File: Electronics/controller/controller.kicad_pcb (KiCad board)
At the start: 2 copper layers, 23 parts, among them P3 PANEL_2, P4 PANEL_1, P5 DIAL, P6 POWER, P7 SWITCH, P8 LED_DISPLAY, Q1 BUZ11, U1 LM317T, U2 74HC595, U3 Arduino_Pro_Micro

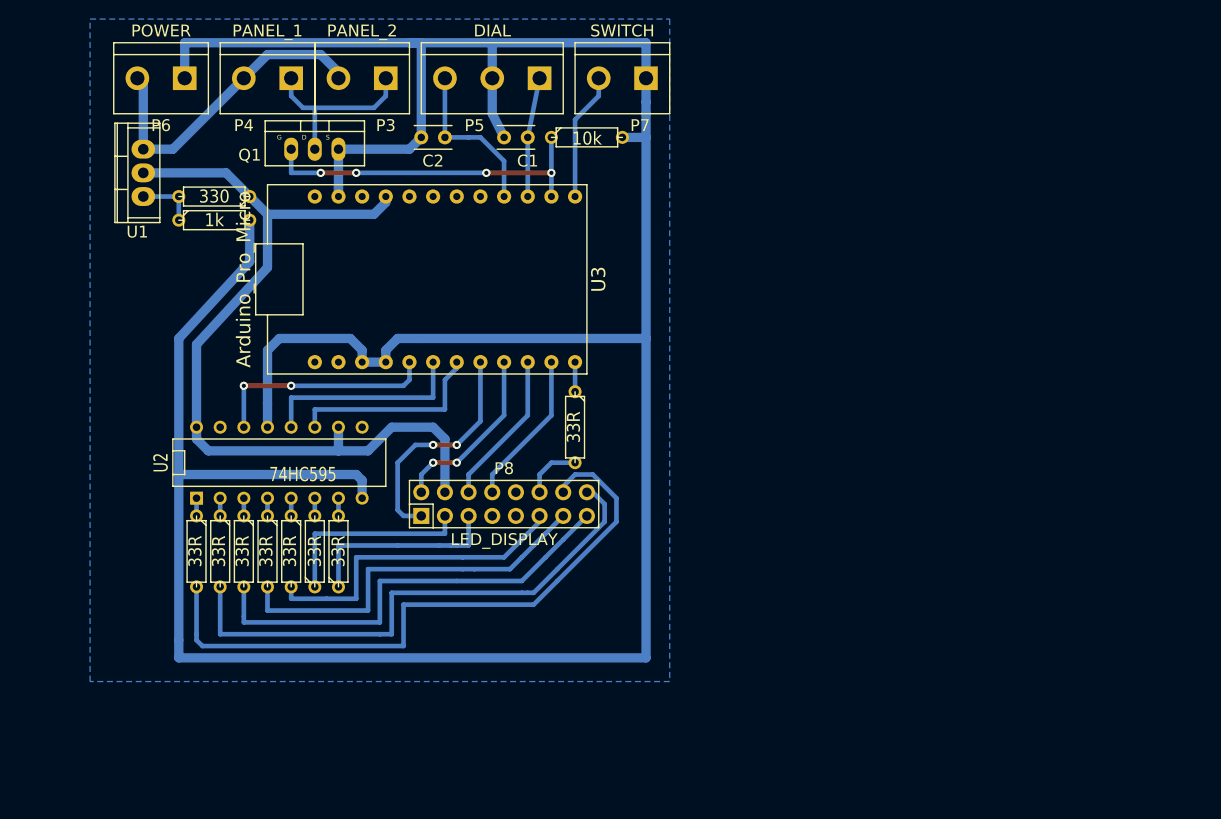
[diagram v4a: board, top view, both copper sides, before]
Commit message: Renumbered some sockets. Rerouted pins.
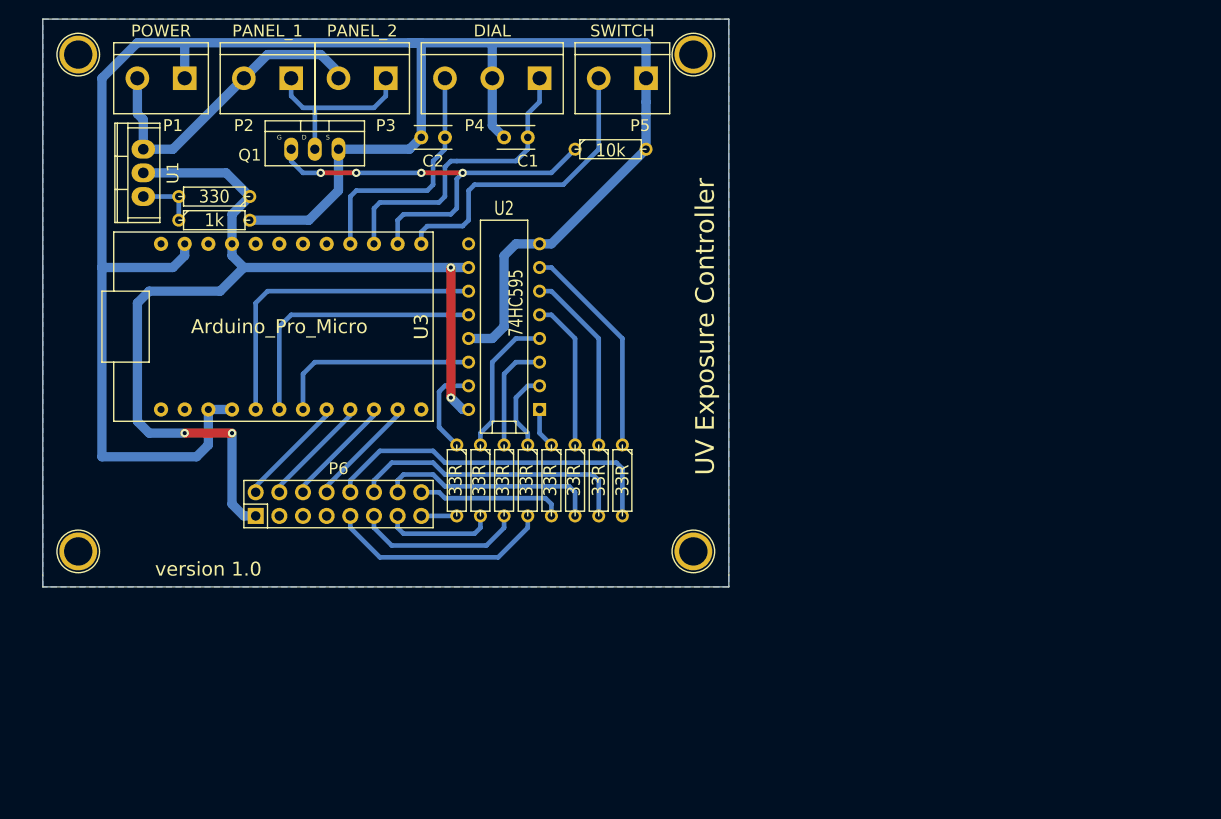
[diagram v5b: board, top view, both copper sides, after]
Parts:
- removed P8: LED_DISPLAY, Pin_Headers:Pin_Header_Straight_2x08
- removed the R10 at (161.3, 95.9)
- removed the R2 at (133.3, 109.2)
- removed the R3 at (135.9, 109.2)
- added 1PIN: P***, Connect:1pin, F.Cu at (174.0, 55.9)
- added 1PIN: P***, Connect:1pin, F.Cu at (108.0, 55.9)
- added 1PIN: P***, Connect:1pin, F.Cu at (174.0, 109.2)
- added 1PIN: P***, Connect:1pin, F.Cu at (108.0, 109.2)
- added P6: LED_DISPLAY, Pin_Headers:Pin_Header_Straight_2x08, F.Cu at (135.9, 104.1)
- added R1: 33R, Discret:R3, F.Cu at (148.6, 101.6)
- added R7: 33R, Discret:R3, F.Cu at (163.8, 101.6)
- added R8: 33R, Discret:R3, F.Cu at (166.4, 101.6)
- moved R6 41.3 mm to (161.3, 101.6)
- moved R5 36.4 mm to (158.8, 101.6)
- moved R3 29.0 mm to (153.7, 101.6)
- moved U2 28.2 mm to (153.7, 85.1), turned to 90 degrees
- moved R4 26.5 mm to (156.2, 101.6)
- moved R2 24.1 mm to (151.1, 101.6)
- moved U3 17.3 mm to (121.9, 83.8)
- moved R9 2.84 mm to (165.1, 66.0)
- renumbered P6 to P1, P4 to P2, P5 to P4, P7 to P5, R5 to R10, R4 to R11, R9 to R2, R7 to R3, R11 to R4, R6 to R5, R8 to R6, R1 to R9
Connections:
- R2 pad 1: /C -> /D
- R3 pad 1: /G -> /C
- R4 pad 1: /F -> /B
- R5 pad 1: /B -> /A
- R6 pad 1: /A -> /E
- U2 pad 11: /D4 -> /D2
- U2 pad 14: /D2 -> /D4
- U2 pad 15: Net-(U2-Pad15) -> /COL
- U2 pad 3: /G -> /C
- U2 pad 4: /C -> /D
- U2 pad 5: /F -> /E
- U2 pad 6: /D -> /F
- U2 pad 7: /E -> /G
- U2 pad 9: Net-(U2-Pad9) -> (no net)
- U3 pad 1: Net-(U3-Pad1) -> (no net)
- U3 pad 10: /D7 -> /D6
- U3 pad 11: /D8 -> /D5
- U3 pad 12: /D9 -> (no net)
- U3 pad 17: Net-(U3-Pad17) -> (no net)
- U3 pad 18: Net-(U3-Pad18) -> (no net)
- U3 pad 19: Net-(U3-Pad19) -> (no net)
- U3 pad 2: Net-(U3-Pad2) -> (no net)
- U3 pad 20: Net-(U3-Pad20) -> (no net)
- U3 pad 22: Net-(U3-Pad22) -> (no net)
- U3 pad 24: Net-(U3-Pad24) -> (no net)
- U3 pad 8: /D5 -> /D8
- U3 pad 9: /D6 -> /D7
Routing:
- net GND: track 335.9 -> 224.3 mm
- net Net-(P6-Pad14): track 69.7 -> 23.9 mm
- net Net-(P6-Pad16): track 58.3 -> 15.8 mm
- net Net-(P6-Pad10): track 0.00 -> 37.7 mm
- net Net-(P6-Pad12): track 0.00 -> 31.1 mm
- net Net-(P6-Pad11): track 48.0 -> 18.1 mm
- net Net-(P6-Pad13): track 41.1 -> 12.0 mm
- net Net-(P8-Pad5): track 21.6 -> 0.00 mm
- net Net-(P8-Pad3): track 21.6 -> 0.00 mm
- net /G: track 1.91 -> 23.5 mm
- net /D14: track 12.8 -> 33.0 mm
- net /D10: track 13.8 -> 33.5 mm
- net /F: track 1.91 -> 19.9 mm
- net VCC: track 93.2 -> 109.0 mm, vias 0 -> 4
- net /E: track 1.91 -> 16.3 mm
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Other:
- board outline added: 73.7 x 61 mm
- board text added: "UV Exposure Controller"
- board text added: "version 1.0"

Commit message: Updates
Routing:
- net Net-(P6-Pad12): track 31.1 -> 27.7 mm
- net Net-(P6-Pad14): track 23.9 -> 21.6 mm
- net Net-(P6-Pad11): track 18.1 -> 16.1 mm
- net Net-(P6-Pad10): track 37.7 -> 35.8 mm
- net Net-(P6-Pad13): track 12.0 -> 10.4 mm
- net GND: track 224.3 -> 222.8 mm
- net Net-(P6-Pad9): track 24.2 -> 23.3 mm
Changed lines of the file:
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@@
     (links 54)
     (no_connects 0)
-    (area 99.735 48.3 182.205 116.8)
+    (area 104.089999 52.019999 177.850001 113.080001)
     (thickness 1.6)
     (drawings 10)
-    (tracks 229)
+    (tracks 226)
     (zones 0)
     (modules 27)
@@
     (pad_to_mask_clearance 0)
     (aux_axis_origin 0 0)
-    (visible_elements 7FFFEFFF)
+    (visible_elements 7FFFFFFF)
     (pcbplotparams
       (layerselection 0x00000_80000001)
@@
   (segment (start 158.75 76.2) (end 168.91 66.04) (width 1) (layer B.Cu) (net 1))
   (segment (start 124.46 93.98) (end 121.92 93.98) (width 1) (layer B.Cu) (net 1))
-  (segment (start 121.92 93.98) (end 121.92 97.79) (width 1) (layer B.Cu) (net 1))
-  (segment (start 121.92 97.79) (end 120.65 99.06) (width 1) (layer B.Cu) (net 1))
-  (segment (start 110.49 78.74) (end 110.49 99.06) (width 1) (layer B.Cu) (net 1))
-  (segment (start 110.49 99.06) (end 120.65 99.06) (width 1) (layer B.Cu) (net 1))
   (segment (start 119.38 76.2) (end 119.38 77.47) (width 1) (layer B.Cu) (net 1))
   (segment (start 118.11 78.74) (end 110.49 78.74) (width 1) (layer B.Cu) (net 1))
@@
   (segment (start 119.38 54.61) (end 119.38 58.42) (width 1) (layer B.Cu) (net 1) (status 20))
   (segment (start 168.91 66.04) (end 168.91 66.04) (width 1) (layer B.Cu) (net 1) (status 10))
-  (segment (start 168.91 62.23) (end 168.91 66.04) (width 1) (layer B.Cu) (net 1) (status 20))
-  (segment (start 168.91 60.96) (end 168.91 62.23) (width 1) (layer B.Cu) (net 1))
-  (segment (start 168.91 54.61) (end 168.91 60.96) (width 1) (layer B.Cu) (net 1))
-  (segment (start 152.4 54.61) (end 168.91 54.61) (width 1) (layer B.Cu) (net 1))
   (segment (start 168.91 66.04) (end 168.91 66.04) (width 1) (layer B.Cu) (net 1) (status 30))
   (segment (start 152.4 54.61) (end 143.51 54.61) (width 1) (layer B.Cu) (net 1))
+  (segment (start 121.92 97.79) (end 121.92 93.98) (width 1) (layer B.Cu) (net 1))
+  (segment (start 120.65 99.06) (end 121.92 97.79) (width 1) (layer B.Cu) (net 1))
+  (segment (start 111.76 99.06) (end 120.65 99.06) (width 1) (layer B.Cu) (net 1))
+  (segment (start 110.49 97.79) (end 111.76 99.06) (width 1) (layer B.Cu) (net 1))
+  (segment (start 110.49 78.74) (end 110.49 97.79) (width 1) (layer B.Cu) (net 1))
+  (segment (start 168.91 62.23) (end 168.91 66.04) (width 1) (layer B.Cu) (net 1))
+  (segment (start 168.91 55.88) (end 168.91 62.23) (width 1) (layer B.Cu) (net 1))
+  (segment (start 167.64 54.61) (end 168.91 55.88) (width 1) (layer B.Cu) (net 1))
+  (segment (start 152.4 54.61) (end 167.64 54.61) (width 1) (layer B.Cu) (net 1))
   (segment (start 149.86 81.28) (end 128.27 81.28) (width 0.5) (layer B.Cu) (net 2))
   (segment (start 128.27 81.28) (end 127 82.55) (width 0.5) (layer B.Cu) (net 2))
@@
   (segment (start 130.81 58.42) (end 130.81 60.325) (width 0.5) (layer B.Cu) (net 24))
   (segment (start 133.35 66.04) (end 133.35 61.595) (width 0.5) (layer B.Cu) (net 24))
-  (segment (start 137.16 105.41) (end 137.16 106.68) (width 0.5) (layer B.Cu) (net 25) (status 10))
+  (segment (start 137.16 106.68) (end 139.192 108.712) (width 0.5) (layer B.Cu) (net 25))
+  (segment (start 154.178 108.712) (end 156.21 106.68) (width 0.5) (layer B.Cu) (net 25))
+  (segment (start 137.16 105.41) (end 137.16 106.68) (width 0.5) (layer B.Cu) (net 25))
+  (segment (start 139.192 108.712) (end 154.178 108.712) (width 0.5) (layer B.Cu) (net 25))
   (segment (start 156.21 106.68) (end 156.21 105.41) (width 0.5) (layer B.Cu) (net 25))
-  (segment (start 153.035 109.855) (end 156.21 106.68) (width 0.5) (layer B.Cu) (net 25))
-  (segment (start 140.335 109.855) (end 153.035 109.855) (width 0.5) (layer B.Cu) (net 25))
-  (segment (start 137.16 106.68) (end 140.335 109.855) (width 0.5) (layer B.Cu) (net 25))
-  (segment (start 137.16 101.6) (end 137.16 102.87) (width 0.5) (layer B.Cu) (net 26) (status 20))
-  (segment (start 140.335 98.425) (end 137.16 101.6) (width 0.5) (layer B.Cu) (net 26))
-  (segment (start 146.05 98.425) (end 140.335 98.425) (width 0.5) (layer B.Cu) (net 26))
-  (segment (start 147.32 99.695) (end 146.05 98.425) (width 0.5) (layer B.Cu) (net 26))
-  (segment (start 165.735 99.695) (end 147.32 99.695) (width 0.5) (layer B.Cu) (net 26))
-  (segment (start 166.37 100.33) (end 165.735 99.695) (width 0.5) (layer B.Cu) (net 26))
-  (segment (start 166.37 105.41) (end 166.37 100.33) (width 0.5) (layer B.Cu) (net 26))
-  (segment (start 139.7 105.41) (end 139.7 106.68) (width 0.5) (layer B.Cu) (net 27) (status 10))
-  (segment (start 139.7 106.68) (end 141.605 108.585) (width 0.5) (layer B.Cu) (net 27))
-  (segment (start 141.605 108.585) (end 151.765 108.585) (width 0.5) (layer B.Cu) (net 27))
-  (segment (start 151.765 108.585) (end 153.67 106.68) (width 0.5) (layer B.Cu) (net 27))
-  (segment (start 153.67 106.68) (end 153.67 105.41) (width 0.5) (layer B.Cu) (net 27))
-  (segment (start 139.7 101.6) (end 139.7 102.87) (width 0.5) (layer B.Cu) (net 28) (status 20))
-  (segment (start 141.605 99.695) (end 139.7 101.6) (width 0.5) (layer B.Cu) (net 28))
-  (segment (start 146.05 99.695) (end 141.605 99.695) (width 0.5) (layer B.Cu) (net 28))
-  (segment (start 147.32 100.965) (end 146.05 99.695) (width 0.5) (layer B.Cu) (net 28))
-  (segment (start 163.195 100.965) (end 147.32 100.965) (width 0.5) (layer B.Cu) (net 28))
-  (segment (start 163.83 101.6) (end 163.195 100.965) (width 0.5) (layer B.Cu) (net 28))
-  (segment (start 163.83 105.41) (end 163.83 101.6) (width 0.5) (layer B.Cu) (net 28))
+  (segment (start 166.37 105.41) (end 166.37 101.854) (width 0.5) (layer B.Cu) (net 26))
+  (segment (start 166.37 101.854) (end 165.608 101.092) (width 0.5) (layer B.Cu) (net 26))
+  (segment (start 148.717 101.092) (end 147.193 99.568) (width 0.5) (layer B.Cu) (net 26))
+  (segment (start 165.608 101.092) (end 148.717 101.092) (width 0.5) (layer B.Cu) (net 26))
+  (segment (start 147.193 99.568) (end 139.192 99.568) (width 0.5) (layer B.Cu) (net 26))
+  (segment (start 139.192 99.568) (end 137.16 101.6) (width 0.5) (layer B.Cu) (net 26))
+  (segment (start 137.16 101.6) (end 137.16 102.87) (width 0.5) (layer B.Cu) (net 26))
+  (segment (start 152.971501 106.108499) (end 153.67 105.41) (width 0.5) (layer B.Cu) (net 27))
+  (segment (start 142.24799 107.95799) (end 151.12201 107.95799) (width 0.5) (layer B.Cu) (net 27))
+  (segment (start 139.7 105.41) (end 142.24799 107.95799) (width 0.5) (layer B.Cu) (net 27))
+  (segment (start 151.12201 107.95799) (end 152.971501 106.108499) (width 0.5) (layer B.Cu) (net 27))
+  (segment (start 163.83 105.41) (end 160.26601 101.84601) (width 0.5) (layer B.Cu) (net 28))
+  (segment (start 140.563599 102.006401) (end 139.7 102.87) (width 0.5) (layer B.Cu) (net 28))
+  (segment (start 146.67701 100.32201) (end 142.24799 100.32201) (width 0.5) (layer B.Cu) (net 28))
+  (segment (start 142.24799 100.32201) (end 140.563599 102.006401) (width 0.5) (layer B.Cu) (net 28))
+  (segment (start 160.26601 101.84601) (end 148.20101 101.84601) (width 0.5) (layer B.Cu) (net 28))
+  (segment (start 148.20101 101.84601) (end 146.67701 100.32201) (width 0.5) (layer B.Cu) (net 28))
   (segment (start 163.576 105.156) (end 163.83 105.41) (width 0.5) (layer B.Cu) (net 28))
-  (segment (start 151.13 106.68) (end 151.13 105.41) (width 0.5) (layer B.Cu) (net 29))
-  (segment (start 150.495 107.315) (end 151.13 106.68) (width 0.5) (layer B.Cu) (net 29))
-  (segment (start 142.875 107.315) (end 150.495 107.315) (width 0.5) (layer B.Cu) (net 29))
-  (segment (start 142.24 106.68) (end 142.875 107.315) (width 0.5) (layer B.Cu) (net 29))
-  (segment (start 142.24 105.41) (end 142.24 106.68) (width 0.5) (layer B.Cu) (net 29) (status 10))
-  (segment (start 161.29 102.87) (end 161.29 105.41) (width 0.5) (layer B.Cu) (net 30))
-  (segment (start 160.655 102.235) (end 161.29 102.87) (width 0.5) (layer B.Cu) (net 30))
-  (segment (start 147.32 102.235) (end 160.655 102.235) (width 0.5) (layer B.Cu) (net 30))
-  (segment (start 147.32 102.235) (end 146.05 100.965) (width 0.5) (layer B.Cu) (net 30))
-  (segment (start 142.875 100.965) (end 146.05 100.965) (width 0.5) (layer B.Cu) (net 30))
-  (segment (start 142.24 101.6) (end 142.875 100.965) (width 0.5) (layer B.Cu) (net 30))
-  (segment (start 142.24 102.87) (end 142.24 101.6) (width 0.5) (layer B.Cu) (net 30) (status 10))
+  (segment (start 150.431501 106.108499) (end 151.13 105.41) (width 0.5) (layer B.Cu) (net 29))
+  (segment (start 149.33602 107.20398) (end 150.431501 106.108499) (width 0.5) (layer B.Cu) (net 29))
+  (segment (start 144.03398 107.20398) (end 149.33602 107.20398) (width 0.5) (layer B.Cu) (net 29))
+  (segment (start 142.24 105.41) (end 144.03398 107.20398) (width 0.5) (layer B.Cu) (net 29))
+  (segment (start 147.68502 102.60002) (end 158.48002 102.60002) (width 0.5) (layer B.Cu) (net 30))
+  (segment (start 144.03398 101.07602) (end 146.16102 101.07602) (width 0.5) (layer B.Cu) (net 30))
+  (segment (start 158.48002 102.60002) (end 160.591501 104.711501) (width 0.5) (layer B.Cu) (net 30))
+  (segment (start 160.591501 104.711501) (end 161.29 105.41) (width 0.5) (layer B.Cu) (net 30))
+  (segment (start 142.24 102.87) (end 144.03398 101.07602) (width 0.5) (layer B.Cu) (net 30))
+  (segment (start 146.16102 101.07602) (end 147.68502 102.60002) (width 0.5) (layer B.Cu) (net 30))
   (segment (start 142.24 102.87) (end 142.24 102.87) (width 0.5) (layer B.Cu) (net 30) (status 30))
   (segment (start 142.24 102.87) (end 142.24 102.87) (width 0.5) (layer B.Cu) (net 30) (status 30))
